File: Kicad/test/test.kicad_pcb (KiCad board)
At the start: 4 copper layers, 46.8 x 47.5 mm, 74 parts, among them J1 SPKOUT, J2 Tag Con, P1 USB_C_Plug_USB2.0, SW1 SW_Push, SW2 SW_Push, SW4 SW_Push, SW5 SW_Push, U1 MAX98357A, U2 ESP32-S3-WROOM-1, U3 OV5640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

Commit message: Routing 80% Done
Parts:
- C29, R14: moved to B.Cu
- moved C29 27.5 mm to (97.7, 41.4), turned to -140 degrees
- moved R14 23.8 mm to (96.6, 40.6), turned to 40 degrees
- moved R8 15.0 mm to (89.5, 48.0)
- moved JP2 6.55 mm to (85.2, 75.7), turned to -90 degrees
- moved C27 3.71 mm to (72.3, 39.0)
- moved R12 1.60 mm to (73.6, 39.5), turned to 90 degrees
- moved JP3 1.35 mm to (67.0, 54.7), turned to 180 degrees
- moved R10 1.23 mm to (70.2, 48.1), turned to 0 degrees
- moved R9 1.14 mm to (86.1, 48.0), turned to 180 degrees
- moved SW4 1.08 mm to (75.6, 72.9)
- moved C28 1.06 mm to (76.5, 73.4)
- moved R13 0.82 mm to (74.4, 72.0)
- moved C25 0.43 mm to (75.3, 55.9)
- moved 3v3J2 0.43 mm to (71.6, 54.3)
- moved C26 0.43 mm to (73.7, 56.0)
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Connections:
- U2 pad 38: SW_L3 -> SW_L2
- U2 pad 39: SW_L2 -> SW_L3
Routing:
- net CAM_VSYNC: track 50.3 -> 0.00 mm, vias 2 -> 0
- net PMIC_IRQ: track 0.00 -> 46.5 mm, vias 0 -> 2
- net CAM_SCL: track 48.1 -> 13.8 mm, vias 3 -> 1
- net CAM_SDA: track 44.0 -> 12.5 mm, vias 2 -> 1
- net SW_L2: track 7.77 -> 39.3 mm, vias 1 -> 0
- net SW_L3: track 8.49 -> 25.0 mm, vias 1 -> 0
- net GND: track 64.9 -> 75.6 mm, vias 55 -> 57
- net +1V5: track 10.5 -> 0.00 mm, vias 2 -> 0
- net TXD: track 34.0 -> 28.2 mm, vias 3 -> 2
- net Net-(JP2-A): track 8.86 -> 14.6 mm
- net PMIC_PWRON: track 27.7 -> 33.3 mm
- net +3V3: track 15.6 -> 10.6 mm, vias 1 -> 5
- net RXD: track 33.3 -> 28.3 mm, vias 3 -> 2
- net BCLK_AMP: track 12.5 -> 10.1 mm
- net GPIO0: track 31.8 -> 29.8 mm
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
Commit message: Routing 95% done
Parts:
- J1: moved to B.Cu
- moved R9 17.3 mm to (85.9, 65.2), turned to 90 degrees
- moved R8 16.9 mm to (87.6, 64.8), turned to 90 degrees
- moved U2 0.39 mm to (73.7, 44.7)
- moved C9 0.26 mm to (97.8, 49.6)
- moved J1 0.23 mm to (76.3, 69.0), turned to -30 degrees
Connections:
- U2 pad 10: CAM_Y2 -> CAM_Y7
- U2 pad 11: CAM_Y3 -> CAM_Y8
- U2 pad 12: CAM_HREF -> CAM_MCLK
- U2 pad 13: CAM_Y5 -> CAM_Y9
- U2 pad 14: CAM_Y6 -> CAM_HREF
- U2 pad 15: CAM_Y7 -> CAM_PWDN
- U2 pad 17: CAM_PCLK -> CAM_SCL
- U2 pad 18: CAM_MCLK -> CAM_SDA
- U2 pad 5: CAM_Y8 -> CAM_Y3
- U2 pad 6: CAM_Y9 -> CAM_Y5
- U2 pad 7: CAM_SCL -> CAM_Y2
- U2 pad 8: CAM_SDA -> CAM_Y6
- U2 pad 9: CAM_PWDN -> CAM_PCLK
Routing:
- net CAM_SDA: track 12.5 -> 38.0 mm
- net CAM_SCL: track 13.8 -> 36.0 mm
- net CAM_Y2: track 0.00 -> 21.6 mm, vias 0 -> 1
- net GPIO46: track 0.00 -> 21.6 mm, vias 0 -> 2
- net CAM_Y9: track 39.8 -> 20.3 mm, vias 2 -> 1
- net CAM_PCLK: track 3.73 -> 20.8 mm, vias 0 -> 1
- net CAM_MCLK: track 0.00 -> 13.3 mm, vias 0 -> 1
- net CAM_RESET: track 9.42 -> 0.00 mm, vias 2 -> 0
- net CAM_Y8: track 27.8 -> 18.5 mm, vias 3 -> 1
- net SW_L3: track 25.0 -> 33.8 mm, vias 0 -> 1
- net +1V5: track 0.00 -> 8.72 mm, vias 0 -> 1
- net CAM_PWDN: track 30.1 -> 24.1 mm, vias 3 -> 1
- net CAM_Y3: track 20.1 -> 24.8 mm, vias 2 -> 1
- net CAM_Y7: track 22.2 -> 18.7 mm, vias 3 -> 1
- net GND: track 75.6 -> 72.8 mm, vias 57 -> 55
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
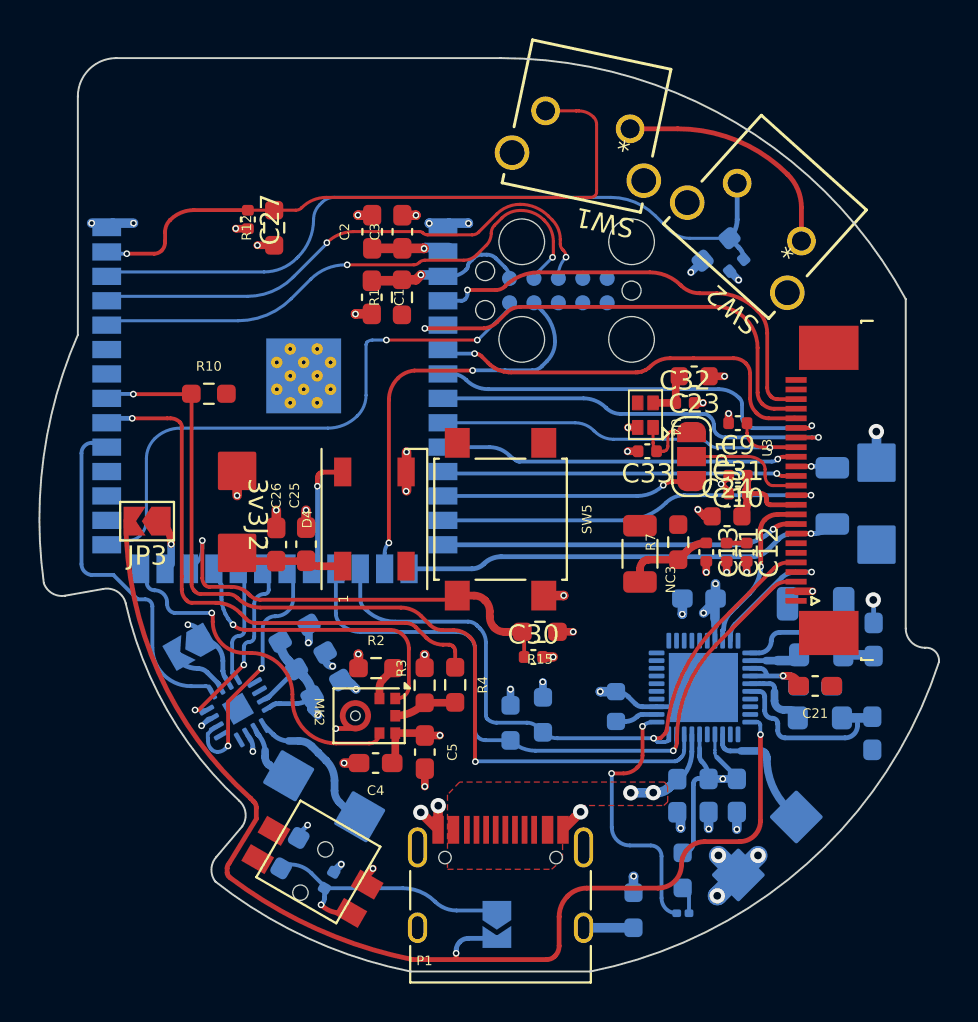
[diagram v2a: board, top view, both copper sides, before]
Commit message: Exposed i2c pads of camera and pmic too and finished routing
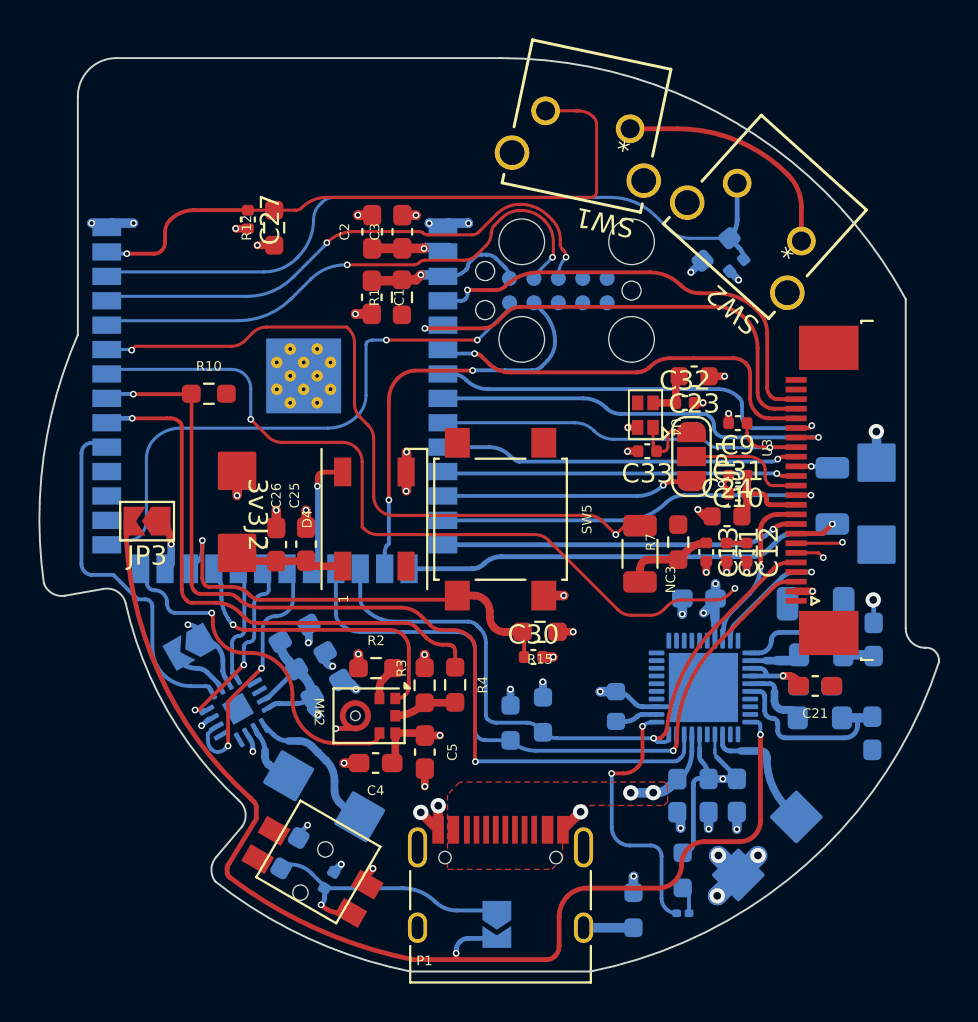
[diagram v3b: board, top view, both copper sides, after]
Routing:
- net CAM_VSYNC: track 0.00 -> 51.9 mm, vias 0 -> 3
- net CAM_RESET: track 0.00 -> 49.8 mm, vias 0 -> 3
- net CAM_PWDN: track 24.1 -> 25.5 mm

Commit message: Zones created Finished Routing
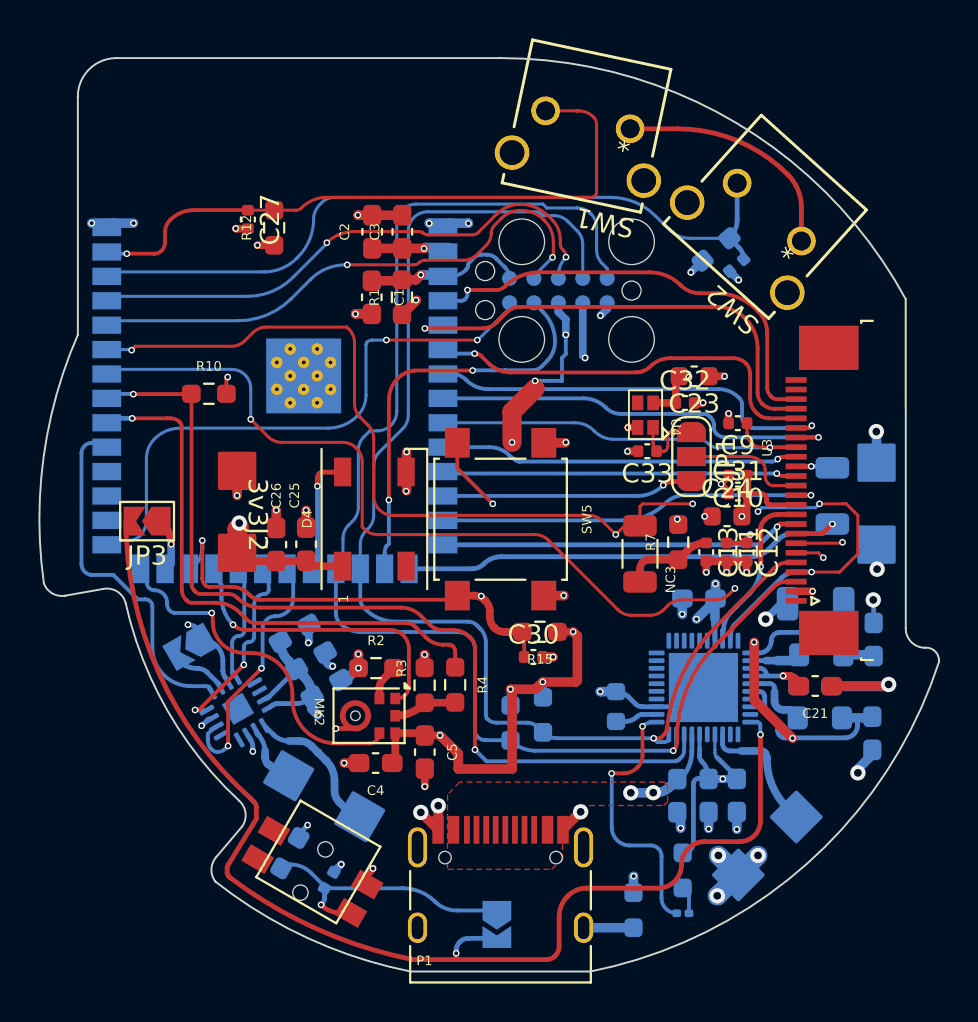
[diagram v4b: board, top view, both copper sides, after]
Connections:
- J2 pad 10: GND -> CAM_SDA
- J2 pad 9: GND -> CAM_SCL
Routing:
- net +3V3: track 13.0 -> 137.1 mm, vias 8 -> 13
- net VSYS: track 35.3 -> 115.5 mm, vias 5 -> 9
- net CAM_SDA: track 38.0 -> 71.9 mm
- net CAM_SCL: track 36.0 -> 66.7 mm
- net +3V3CAM: track 17.5 -> 43.4 mm, vias 0 -> 5
- net +2V8: track 7.82 -> 20.4 mm, vias 1 -> 4
- net GND: track 72.8 -> 84.7 mm, vias 55 -> 58
- net SW_L1: track 23.0 -> 32.0 mm, vias 1 -> 3
- net CAM_RESET: track 49.8 -> 51.4 mm, vias 3 -> 4
- added copper zone on In2.Cu, net +3V3
- added copper zone on In2.Cu, net VSYS

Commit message: Finished layouts and offsetting
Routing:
- net +3V3: track 137.1 -> 140.5 mm
- net SW_L1: track 32.0 -> 34.8 mm
- net GPIO0: track 29.9 -> 28.6 mm
- net VSYS: track 115.5 -> 114.4 mm, vias 9 -> 7
- net CAM_RESET: track 51.4 -> 50.9 mm, vias 4 -> 3
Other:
- board text added: "+"
- board text added: "1"
